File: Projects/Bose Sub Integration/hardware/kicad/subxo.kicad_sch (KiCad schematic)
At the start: 44 parts, among them J1 IN L, J2 IN R, J3 OUT 3.5mm, J4 PWR IN 15V, J5 POLARITY SW, J6 LEVEL POT 10k, J7 INV LED, U1 TL074, U2 LM7812

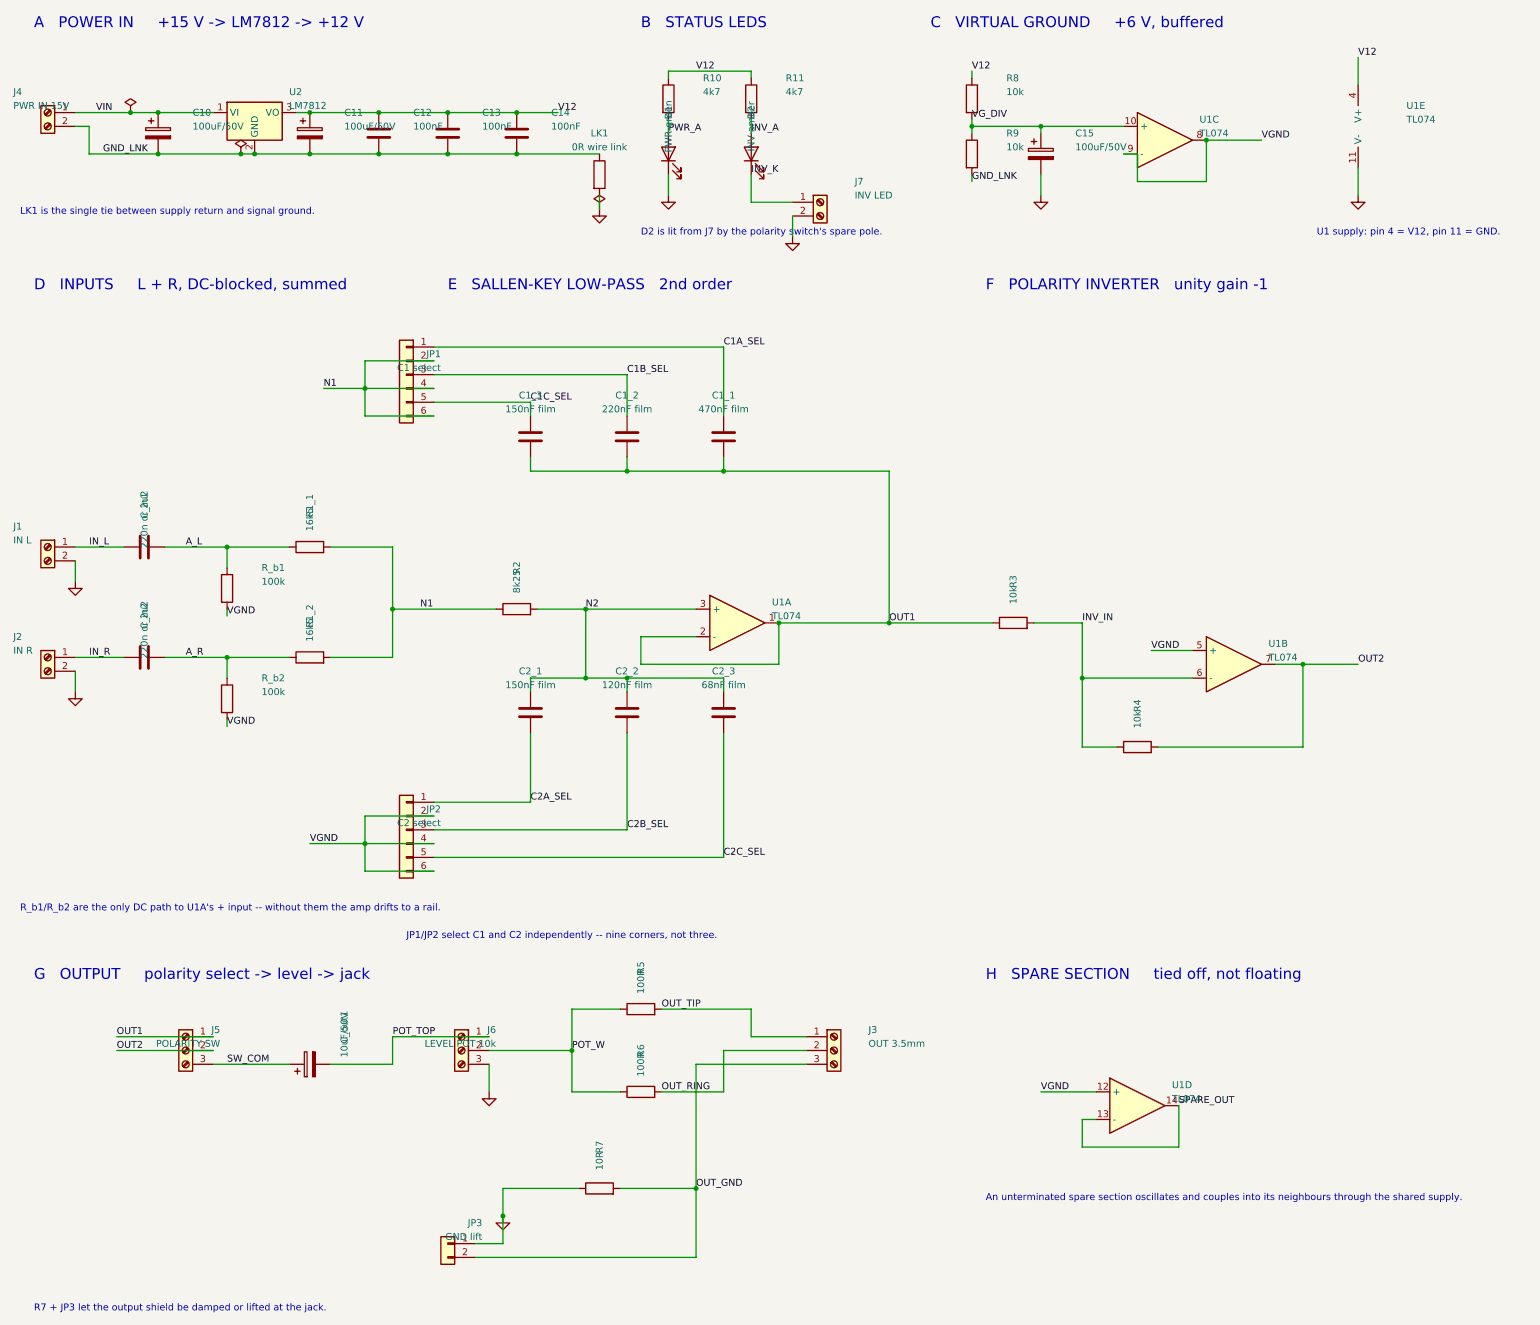
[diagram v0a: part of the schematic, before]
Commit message: Sub crossover: emit the sheet directly, no upgrade pass
Every version tested so far had one of three faults, and each fix was masked by
the next: the first minted its own root uuid instead of the one the project
names; the second had that right but was then run through
"kicad-cli sch upgrade", which rewrites each symbol onto its own instance path;
the third was a retrofit of the original file that sexpdata wrote as a single
line carrying a KiCad 9 header.

This is the combination none of them had at once - generated directly, KiCad 10
format, root uuid 89cbaec3 as the project records it, and all 60 symbols
sharing that one instance path, with no upgrade pass anywhere near it.

ERC --severity-all reports 5 lib_symbol_mismatch, netlist identical at
44 parts / 31 nets / 112 nodes, and the readability checks pass.
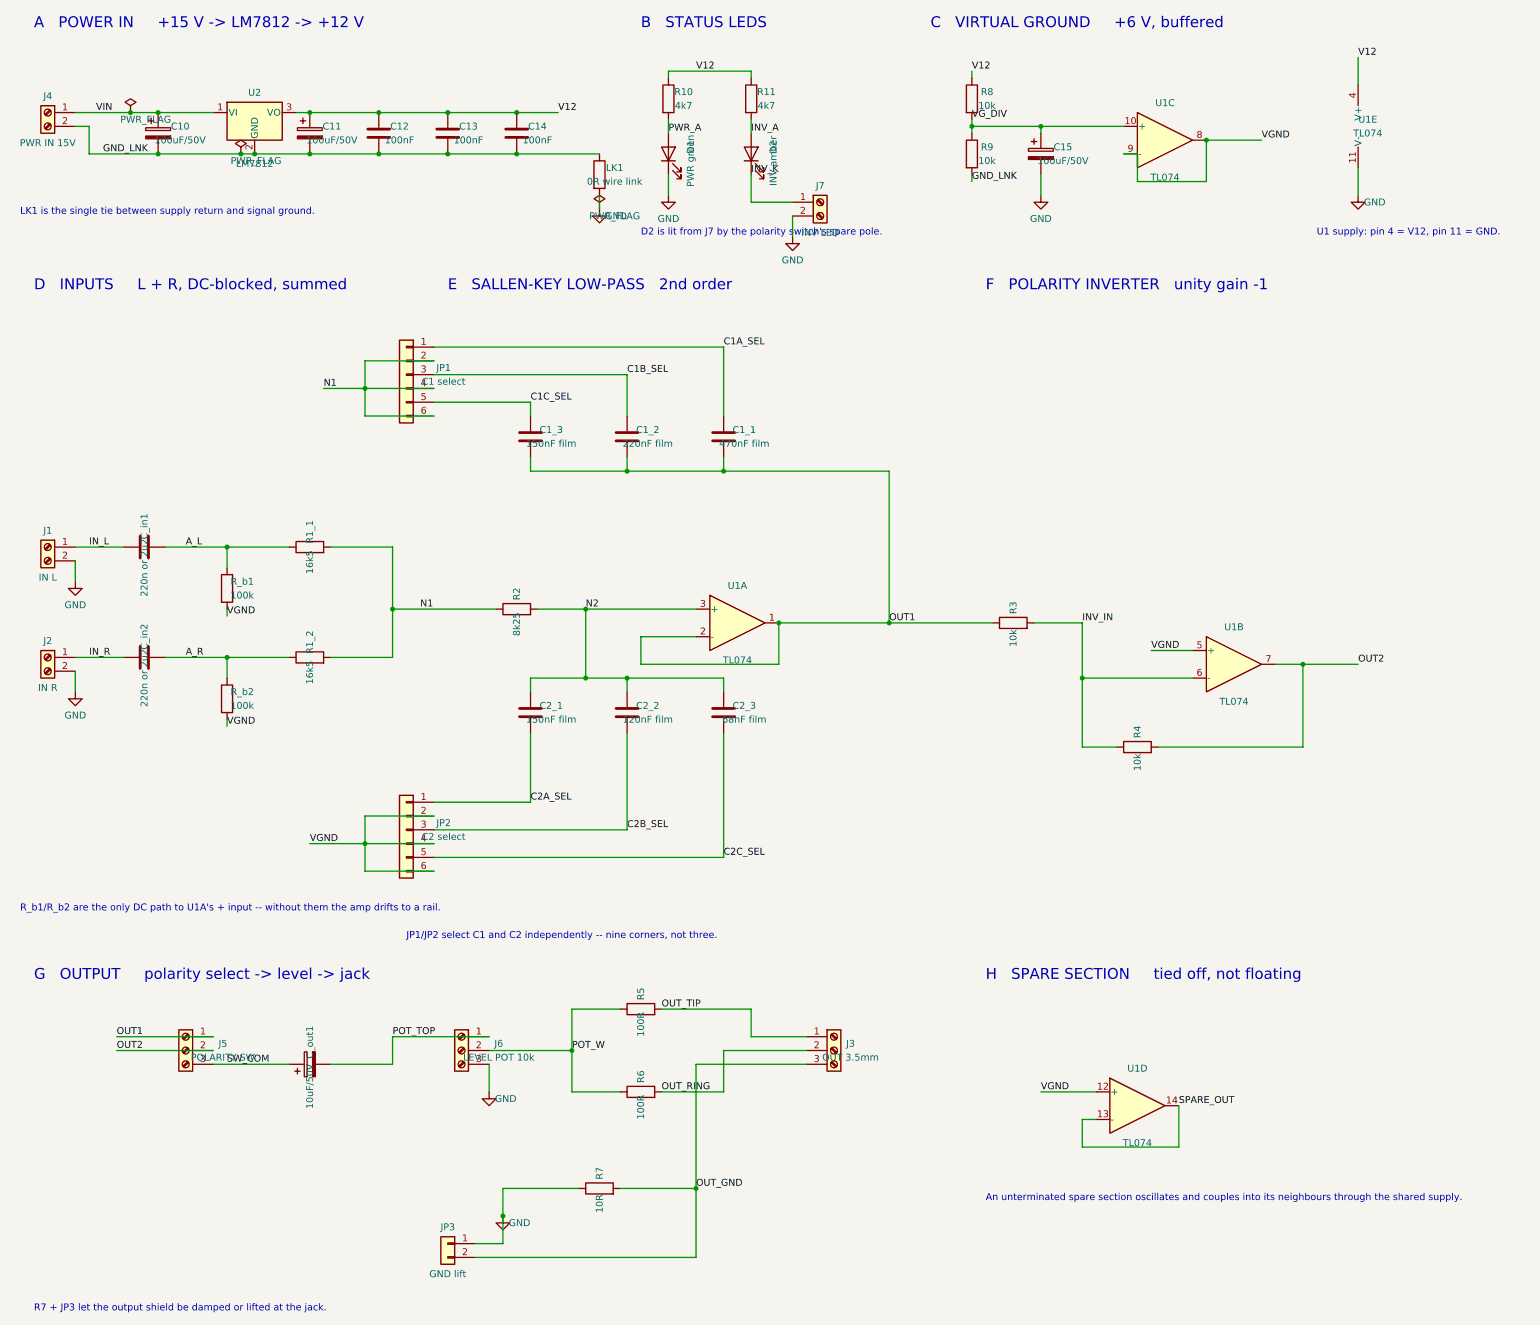
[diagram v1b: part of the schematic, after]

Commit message: Sub crossover: restore the original, keep the redraw as a reference
Seven attempts at generating a schematic Eeschema accepts have failed. Each
version passed everything measurable from outside the GUI - kicad-cli reads the
netlist correctly, ERC --severity-all is clean, no pin sits anywhere but a wire
endpoint - and each still reported unconnected pins when opened. I cannot
reproduce or diagnose that without the GUI, and it is not worth more of the
board owner's time.

The original is back in place, unchanged and building as before.

The redraw is kept as reference material rather than as the board:
  subxo-redraw-reference.kicad_sch  the drawing itself, to open and compare
  subxo-redraw-reference.pdf        what the finished sheet should look like
  subxo-redraw-placement.md         every part's target position, rotation and
                                    mirror, plus the three-band structure

Applying it by hand in Eeschema means KiCad writes every byte, which sidesteps
the whole problem. tools/subxo_layout.py still regenerates the reference.
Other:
- note added: "A POWER IN -> +12 V"
- note added: "A4 is the spare section: + on VGND, out tied to in-. An unterminated spare oscillates and couples into its neighbours through the shared supply."
- note added: "B U1 SUPPLY"
- note added: "Bose Companion 5 sub crossover -- mono-summing 2nd-order Sallen-Key low-pass."
- note added: "C VIRTUAL GROUND 6 V"
- note added: "C1 returns to N1 -- the Sallen-Key feedback path. Not N2. JP1 selects C1 (odd pin = cap, even pin = N1); JP2 selects C2 (odd = cap, even = VGND). They select INDEPENDENTLY -- nine corners, not three pairs. Corners below are MEASURED on the rev A board, not calculated: the quoted f0 = 1/(2*pi*R*sqrt(C1*C2)) is not a -3 dB point, and C_in sits inside the filter. See Results - Sub Crossover Bring-up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"
- note added: "C_in1/C_in2 use a dual-pitch footprint: 5.00 mm for the 220n as built (or a 2u2 non-polarised electrolytic), 15.00 mm for a real 2u2 film part. Fit ONE pair. 220n puts ~8.8k of reactance in series with R1 at 82 Hz, so it is part of the filter, not just an input high-pass -- it costs 1.3-3.1 dB of passband level and damps the peaking. Whether that is a defect or a feature is a listening question; 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"
- note added: "C_out + faces SW_COM: that node sits at 6 V DC, the pot side at 0 V. J6 pin 3 = GND, not VGND -- C_out has already removed the 6 V bias; referencing the pot to VGND would thump the driver at power-on. JP3 shorts R7 (ground lift). Normally fitted."
- note added: "D INPUT L"
- note added: "D1 = power lamp on V12 (proves the LM7812, not just VIN). D2 = INVERTED lamp, fed from SW2's unused second pole via J7. Both ~2 mA. No LED touches a signal node."
- note added: "E INPUT R"
- note added: "F SALLEN-KEY LOW-PASS"
- note added: "G POLARITY INVERTER"
- note added: "H OUTPUT STAGE"
- note added: "I STATUS LEDS"
- note added: "Off-board: level pot (J6), polarity switch (J5), all panel jacks (J1/J2/J3). Process: single-sided THT, bottom copper only, board outline 100 x 100 mm. Copper is isolation-milled on the CNC with an 0.8 mm flat end mill; the fiber laser does the silkscreen only. Routing clearance 0.85 mm / track 1.0 mm. The 0.8 mm tool width is a hard floor on every copper-to-copper gap. Fixed-pitch pads sit below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"
- note added: "R_b1/R_b2 are the only DC path to A1's + input (C_in blocks DC, C2 is a capacitor). Without them A1 drifts to a rail. They sit after the coupling caps -- 100k at N1 would shift every corner by 8%."
- note added: "Reference names vs the handoff document: KiCad treats a reference with no trailing digit as unannotated, so C1a/C1b/C1c -> C1_1/C1_2/C1_3, C2a/C2b/C2c -> C2_1/C2_2/C2_3, R1a/R1b -> R1_1/R1_2, C_out -> C_out1."
- note added: "Single +12 V rail, no negative supply. All AC referenced to VGND = 6 V (A3 buffers the R8/R9 mid-rail divider)."
- note added: "U1 supply: pin 4 = V12, pin 11 = GND. No negative rail."
- note removed: "A POWER IN +15 V -> LM7812 -> +12 V"
- note removed: "An unterminated spare section oscillates and couples into its neighbours through the shared supply."
- note removed: "B STATUS LEDS"
- note removed: "C VIRTUAL GROUND +6 V, buffered"
- note removed: "D INPUTS L + R, DC-blocked, summed"
- note removed: "D2 is lit from J7 by the polarity switch's spare pole."
- note removed: "E SALLEN-KEY LOW-PASS 2nd order"
- note removed: "F POLARITY INVERTER unity gain -1"
- note removed: "G OUTPUT polarity select -> level -> jack"
- note removed: "H SPARE SECTION tied off, not floating"
- note removed: "JP1/JP2 select C1 and C2 independently -- nine corners, not three."
- note removed: "LK1 is the single tie between supply return and signal ground."
- note removed: "R7 + JP3 let the output shield be damped or lifted at the jack."
- note removed: "R_b1/R_b2 are the only DC path to U1A's + input -- without them the amp drifts to a rail."
- note removed: "U1 supply: pin 4 = V12, pin 11 = GND."

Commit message: Sub crossover: put the redrawn schematic back
The netclass fix from the Class D work resolves what blocked this. The Default
netclass in subxo.kicad_pro had no wire_width key, and KiCad 10 applies the
netclass wire width to every wire on the sheet, where a missing key resolves to
zero. Every wire drew at zero width and the junction dots went with them, since
dot size derives from wire width. The sheet looked like disconnected hairlines
while ERC and the netlist were correct the whole time - which is exactly why
every headless check passed while the GUI looked broken.

Confirmed here without a GUI by exporting the same sheet to PDF three times:
alone with no project file, beside the old project file, and beside the fixed
one. The old-project export differs from both others; the fixed one matches the
no-project default. Note that sch export svg does not apply the netclass at all,
so only the PDF route shows it.

The redraw is back as subxo.kicad_sch: netlist identical to the pre-redraw
board at 44 parts / 31 nets / 112 nodes, ERC --severity-all reports 5
lib_symbol_mismatch, and all twelve readability checks pass - 8% stitched
against 97% before, 92% of pins wired to another part against 13%.

The reference copies are removed now that the drawing is the board again.
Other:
- note added: "A POWER IN +15 V -> LM7812 -> +12 V"
- note added: "An unterminated spare section oscillates and couples into its neighbours through the shared supply."
- note added: "B STATUS LEDS"
- note added: "C VIRTUAL GROUND +6 V, buffered"
- note added: "D INPUTS L + R, DC-blocked, summed"
- note added: "D2 is lit from J7 by the polarity switch's spare pole."
- note added: "E SALLEN-KEY LOW-PASS 2nd order"
- note added: "F POLARITY INVERTER unity gain -1"
- note added: "G OUTPUT polarity select -> level -> jack"
- note added: "H SPARE SECTION tied off, not floating"
- note added: "JP1/JP2 select C1 and C2 independently -- nine corners, not three."
- note added: "LK1 is the single tie between supply return and signal ground."
- note added: "R7 + JP3 let the output shield be damped or lifted at the jack."
- note added: "R_b1/R_b2 are the only DC path to U1A's + input -- without them the amp drifts to a rail."
- note added: "U1 supply: pin 4 = V12, pin 11 = GND."
- note removed: "A POWER IN -> +12 V"
- note removed: "A4 is the spare section: + on VGND, out tied to in-. An unterminated spare oscillates and couples into its neighbours through the shared supply."
- note removed: "B U1 SUPPLY"
- note removed: "Bose Companion 5 sub crossover -- mono-summing 2nd-order Sallen-Key low-pass."
- note removed: "C VIRTUAL GROUND 6 V"
- note removed: "C1 returns to N1 -- the Sallen-Key feedback path. Not N2. JP1 selects C1 (odd pin = cap, even pin = N1); JP2 selects C2 (odd = cap, even = VGND). They select INDEPENDENTLY -- nine corners, not three pairs. Corners below are MEASURED on the rev A board, not calculated: the quoted f0 = 1/(2*pi*R*sqrt(C1*C2)) is not a -3 dB point, and C_in sits inside the filter. See Results - Sub Crossover Bring-up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"
- note removed: "C_in1/C_in2 use a dual-pitch footprint: 5.00 mm for the 220n as built (or a 2u2 non-polarised electrolytic), 15.00 mm for a real 2u2 film part. Fit ONE pair. 220n puts ~8.8k of reactance in series with R1 at 82 Hz, so it is part of the filter, not just an input high-pass -- it costs 1.3-3.1 dB of passband level and damps the peaking. Whether that is a defect or a feature is a listening question; 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"
- note removed: "C_out + faces SW_COM: that node sits at 6 V DC, the pot side at 0 V. J6 pin 3 = GND, not VGND -- C_out has already removed the 6 V bias; referencing the pot to VGND would thump the driver at power-on. JP3 shorts R7 (ground lift). Normally fitted."
- note removed: "D INPUT L"
- note removed: "D1 = power lamp on V12 (proves the LM7812, not just VIN). D2 = INVERTED lamp, fed from SW2's unused second pole via J7. Both ~2 mA. No LED touches a signal node."
- note removed: "E INPUT R"
- note removed: "F SALLEN-KEY LOW-PASS"
- note removed: "G POLARITY INVERTER"
- note removed: "H OUTPUT STAGE"
- note removed: "I STATUS LEDS"
- note removed: "Off-board: level pot (J6), polarity switch (J5), all panel jacks (J1/J2/J3). Process: single-sided THT, bottom copper only, board outline 100 x 100 mm. Copper is isolation-milled on the CNC with an 0.8 mm flat end mill; the fiber laser does the silkscreen only. Routing clearance 0.85 mm / track 1.0 mm. The 0.8 mm tool width is a hard floor on every copper-to-copper gap. Fixed-pitch pads sit below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"
- note removed: "R_b1/R_b2 are the only DC path to A1's + input (C_in blocks DC, C2 is a capacitor). Without them A1 drifts to a rail. They sit after the coupling caps -- 100k at N1 would shift every corner by 8%."
- note removed: "Reference names vs the handoff document: KiCad treats a reference with no trailing digit as unannotated, so C1a/C1b/C1c -> C1_1/C1_2/C1_3, C2a/C2b/C2c -> C2_1/C2_2/C2_3, R1a/R1b -> R1_1/R1_2, C_out -> C_out1."
- note removed: "Single +12 V rail, no negative supply. All AC referenced to VGND = 6 V (A3 buffers the R8/R9 mid-rail divider)."
- note removed: "U1 supply: pin 4 = V12, pin 11 = GND. No negative rail."
